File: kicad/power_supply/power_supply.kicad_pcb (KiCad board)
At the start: 2 copper layers, 79.2 x 46.2 mm, 14 parts, among them J1 AC IN, J2 DC OUT

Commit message: Finished power supply
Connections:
- net Net-(D1-A) renamed /AC1
- net Net-(D1-K) renamed /V+
- net Net-(D2-A) renamed /V-
- net Net-(D2-K) renamed /AC2
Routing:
- net /V+: track 64.8 -> 0.00 mm
- net /V-: track 64.3 -> 0.00 mm
- net /AC1: track 39.1 -> 0.00 mm
- net /AC2: track 18.9 -> 0.20 mm
- added copper zone on B.Cu, net /AC1
- added copper zone on B.Cu, net /AC2
- added copper zone on B.Cu, net /V+
- added copper zone on B.Cu, net /V-
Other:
- board text added: "GND"

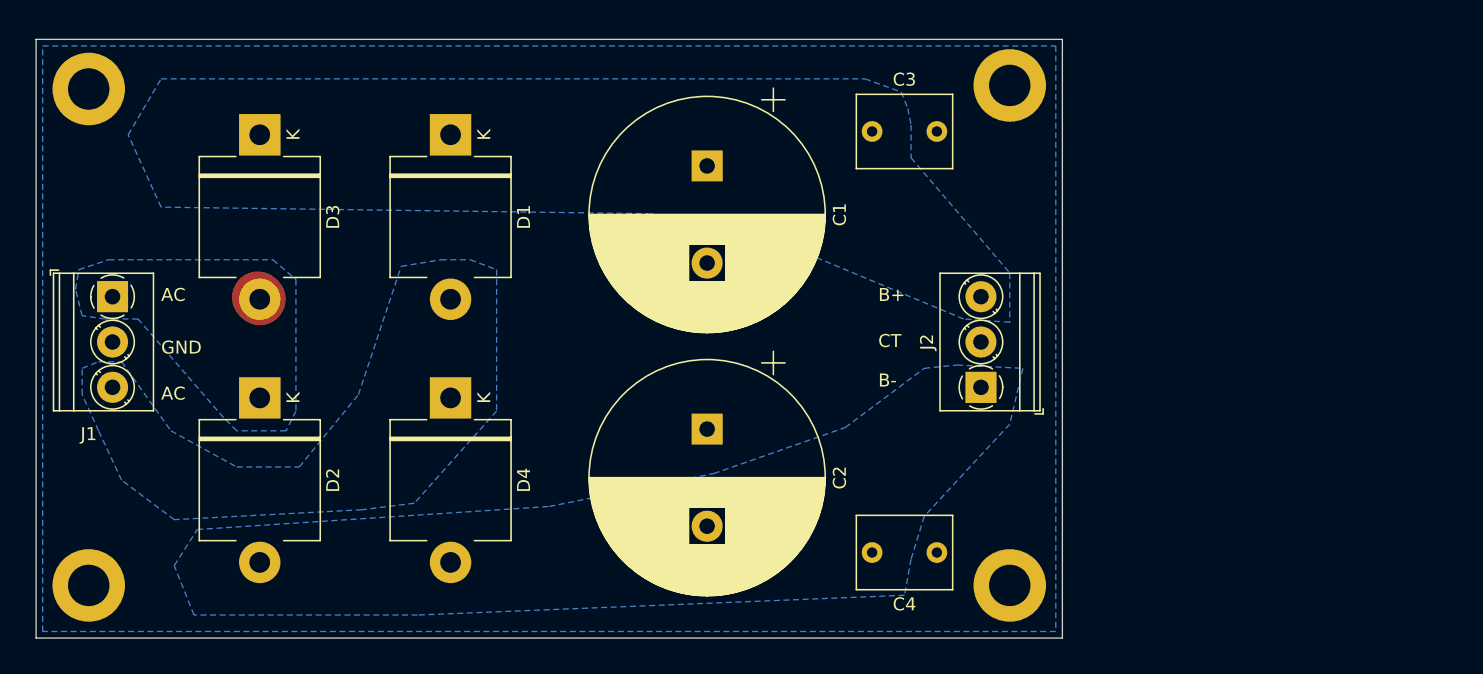
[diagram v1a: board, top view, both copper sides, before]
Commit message: Added images
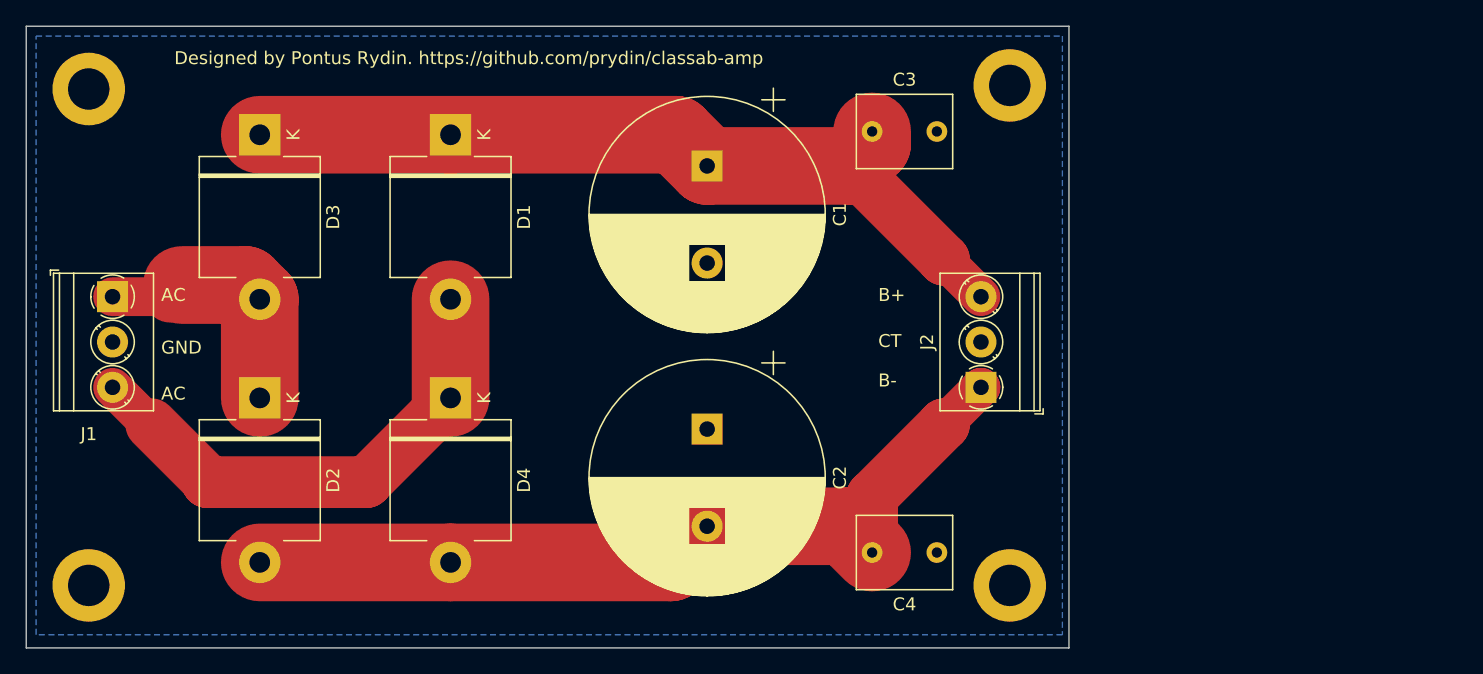
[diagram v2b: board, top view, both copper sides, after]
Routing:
- net /V-: track 0.00 -> 65.5 mm
- net /V+: track 0.00 -> 64.2 mm
- net /AC1: track 0.00 -> 39.5 mm
- net /AC2: track 0.20 -> 19.7 mm
- removed copper zone on B.Cu, net /AC1
- removed copper zone on B.Cu, net /AC2
- removed copper zone on B.Cu, net /V+
- removed copper zone on B.Cu, net /V-
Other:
- board size 79.2 x 46.2 mm -> 80.5 x 48 mm
- board text added: "Designed by Pontus Rydin. https://github.com/prydin/classab-amp"

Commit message: 1.1 RC
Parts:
- added C5: 4700u, Capacitor_THT:CP_Radial_D18.0mm_P7.50mm, F.Cu at (130.0, 72.3)
- added C6: 4700u, Capacitor_THT:CP_Radial_D18.0mm_P7.50mm, F.Cu at (130.0, 93.0)
- moved J2 24.9 mm to (154.7, 89.4)
- moved C3 23.1 mm to (144.5, 69.7)
- moved C4 23.1 mm to (149.5, 102.2)
- moved REF** 23.1 mm to (155.1, 104.7)
- moved REF** 23.1 mm to (155.1, 66.1)
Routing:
- net /V+: track 64.2 -> 89.6 mm
- net /V-: track 65.5 -> 90.9 mm
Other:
- board size 80.5 x 48 mm -> 105.4 x 48 mm

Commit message: Update gerber files
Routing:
- net /V-: track 90.9 -> 86.9 mm
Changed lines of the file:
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@@
 	)
 	(segment
-		(start 146.852 70.564)
-		(end 145.16 72.256)
-		(width 6)
-		(layer "F.Cu")
-		(net 2)
-	)
-	(segment
-		(start 146.852 69.596)
-		(end 146.852 70.564)
+		(start 144.504 69.652)
+		(end 145.16 70.308)
 		(width 6)
 		(layer "F.Cu")
@@
 	)
 	(segment
+		(start 145.16 70.308)
+		(end 145.16 72.256)
+		(width 6)
+		(layer "F.Cu")
+		(net 2)
+	)
+	(segment
 		(start 88.9 102.87)
 		(end 105.918 102.87)
@@
 	)
 	(segment
-		(start 108.712 100.076)
-		(end 144.82 100.076)
-		(width 6)
-		(layer "F.Cu")
-		(net 3)
-	)
-	(segment
-		(start 152.4 92.208)
-		(end 152.4 92.202)
+		(start 146.852 98.044)
+		(end 146.852 97.756)
 		(width 4)
 		(layer "F.Cu")
@@
 	)
 	(segment
-		(start 146.852 102.108)
-		(end 146.852 97.756)
+		(start 144.82 100.076)
+		(end 146.852 98.044)
 		(width 4)
+		(layer "F.Cu")
+		(net 3)
+	)
+	(segment
+		(start 146.852 97.756)
+		(end 152.4 92.208)
+		(width 4)
+		(layer "F.Cu")
+		(net 3)
+	)
+	(segment
+		(start 108.712 100.076)
+		(end 144.82 100.076)
+		(width 6)
 		(layer "F.Cu")
 		(net 3)
@@
 		(end 108.712 100.076)
 		(width 6)
-		(layer "F.Cu")
-		(net 3)
-	)
-	(segment
-		(start 146.852 97.756)
-		(end 152.4 92.208)
-		(width 4)
 		(layer "F.Cu")
 		(net 3)
@@
 	)
 	(segment
-		(start 144.82 100.076)
-		(end 146.852 102.108)
-		(width 6)
+		(start 152.4 92.208)
+		(end 152.4 92.202)
+		(width 4)
 		(layer "F.Cu")
 		(net 3)

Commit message: WIP
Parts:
- added R1: 1k, Resistor_THT:R_Axial_DIN0414_L11.9mm_D4.5mm_P15.24mm_Horizontal, F.Cu at (99.1, 68.1)
- added R2: 1k, Resistor_THT:R_Axial_DIN0414_L11.9mm_D4.5mm_P15.24mm_Horizontal, F.Cu at (99.1, 89.4)
- moved C3 5.59 mm to (150.1, 69.7)
- moved C4 5.59 mm to (155.1, 102.2)
- moved J2 5.59 mm to (160.3, 89.4)
- moved C1 5.59 mm to (114.3, 72.3)
- moved C2 5.59 mm to (114.3, 92.6)
- moved C5 5.59 mm to (135.6, 72.3)
- moved C6 5.59 mm to (135.6, 93.0)
- moved REF** 5.59 mm to (160.7, 104.7)
- moved REF** 5.59 mm to (160.7, 66.1)
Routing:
- net /V-: track 86.9 -> 92.4 mm
- net /V+: track 89.1 -> 94.7 mm
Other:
- board size 105.4 x 48 mm -> 110.5 x 48 mm
